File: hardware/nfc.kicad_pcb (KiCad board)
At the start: 2 copper layers, 85 x 50 mm, 61 parts, among them J1 CONN_01X03, P1 CON-SENSOR2, P2 BOOT, P3 DEBUG, U1 XMC130024, U2 PN7150, U3 DRILL, U4 DRILL, U5 DRILL, U6 DRILL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

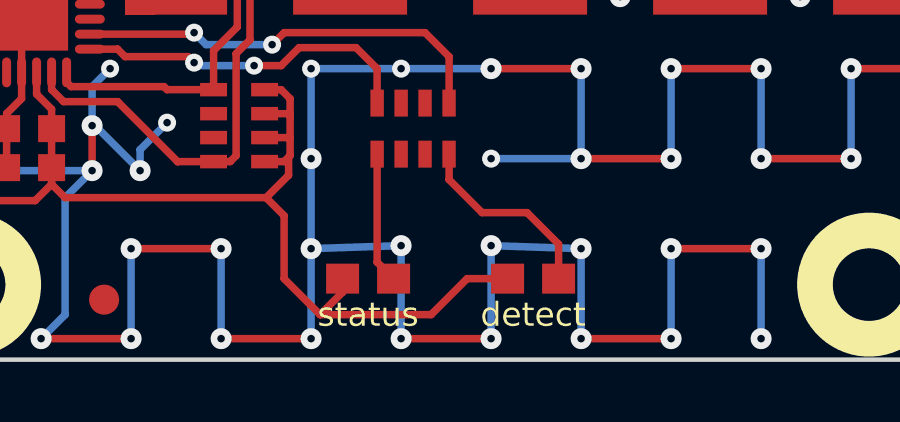
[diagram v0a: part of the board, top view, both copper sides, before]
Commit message: fix led text
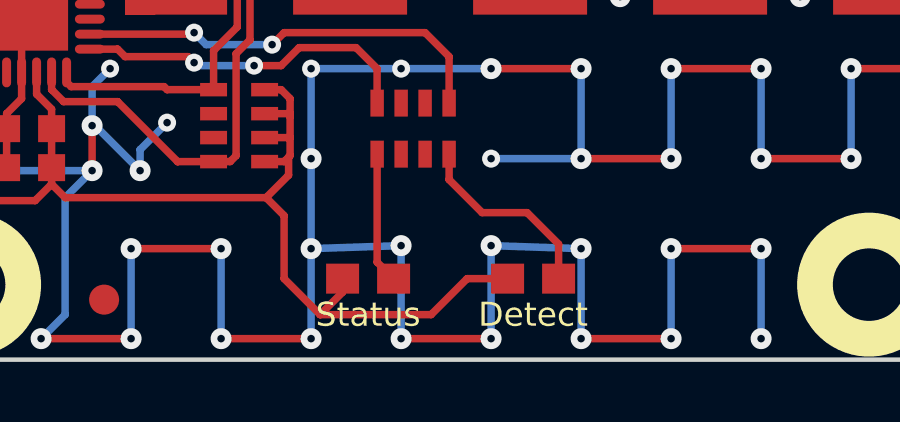
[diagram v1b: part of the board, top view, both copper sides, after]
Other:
- board text added: "Detect"
- board text added: "Status"
- board text removed: "detect"
- board text removed: "status"
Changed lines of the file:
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@@
-(kicad_pcb (version 4) (host pcbnew 4.0.2+dfsg1-stable)
+(kicad_pcb (version 4) (host pcbnew 4.0.7-e2-6376~61~ubuntu18.04.1)
   (general
     (links 136)
     (no_connects 0)
-    (area 110.324999 51.924999 195.475001 102.075001)
+    (area 109.544999 51.144999 275.89286 161.25)
     (thickness 1.6)
     (drawings 13)
@@
     )
   )
-  (gr_text detect (at 131.7 100.5) (layer F.SilkS)
+  (gr_text Detect (at 131.7 100.5) (layer F.SilkS)
     (effects (font (size 0.8 0.8) (thickness 0.15)))
   )
-  (gr_text status (at 126.2 100.5) (layer F.SilkS)
+  (gr_text Status (at 126.2 100.5) (layer F.SilkS)
     (effects (font (size 0.8 0.8) (thickness 0.15)))
   )

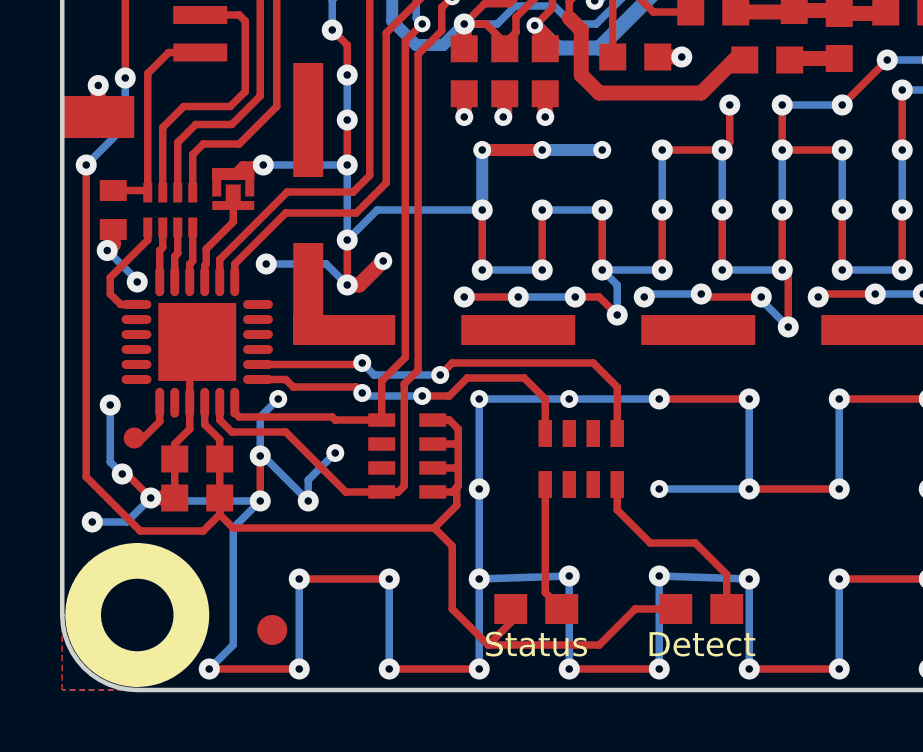
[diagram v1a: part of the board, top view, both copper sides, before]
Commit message: Change capacitor footprint(s) to C0402F
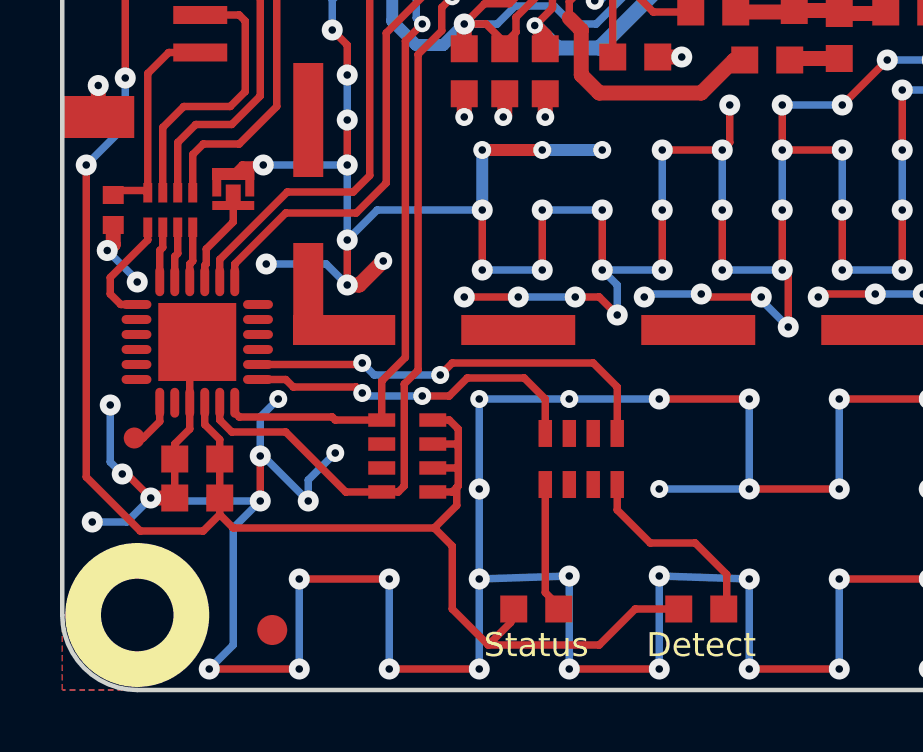
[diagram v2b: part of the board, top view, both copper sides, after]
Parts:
- ANT1: footprint NFC_ANTENNA_40_40 -> kicad-libraries:NFC_ANTENNA_40_40
- C1: footprint C0402E -> kicad-libraries:C0402F
- C10, C12, C13, C14, C15, C16, C17, C18, C19, C20, C21, C22, C23, C24, C25, C3, C4, C5, C6, C7, C8, C9: footprint C0603F -> kicad-libraries:C0603F
- D1, D2: footprint D0603E -> kicad-libraries:D0603F
- L1, L2, R1, R2, R3, R4, R5, R6: footprint R0603F -> kicad-libraries:R0603F
- RP2, RP3: footprint 4X0603 -> kicad-libraries:4X0603
- U3, U4, U5, U6, U7, U8: footprint DRILL_NP -> kicad-libraries:DRILL_NP
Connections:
- RP2 pad 6: (no net) -> Net-(RP2-Pad6)
- RP2 pad 7: (no net) -> Net-(RP2-Pad7)
- RP3 pad 2: (no net) -> Net-(RP3-Pad2)
- RP3 pad 3: (no net) -> Net-(RP3-Pad3)
- RP3 pad 6: (no net) -> Net-(RP3-Pad6)
- RP3 pad 7: (no net) -> Net-(RP3-Pad7)
- U1 pad 15: (no net) -> Net-(U1-Pad15)
- U1 pad 16: (no net) -> Net-(U1-Pad16)
- U1 pad 17: (no net) -> Net-(U1-Pad17)
- U1 pad 18: (no net) -> Net-(U1-Pad18)
- U1 pad 2: (no net) -> Net-(U1-Pad2)
- U1 pad 3: (no net) -> Net-(U1-Pad3)
- U1 pad 4: (no net) -> Net-(U1-Pad4)
- U1 pad 5: (no net) -> Net-(U1-Pad5)
- U1 pad 6: (no net) -> Net-(U1-Pad6)
- U1 pad 8: (no net) -> Net-(U1-Pad8)
- U2 pad 11: (no net) -> Net-(U2-Pad11)
- U2 pad 20: (no net) -> Net-(U2-Pad20)
- U2 pad 23: (no net) -> Net-(U2-Pad23)
- U2 pad 24: (no net) -> Net-(U2-Pad24)
- U2 pad 25: (no net) -> Net-(U2-Pad25)
- U2 pad 31: (no net) -> Net-(U2-Pad31)
- U2 pad 32: (no net) -> Net-(U2-Pad32)
- U2 pad 33: (no net) -> Net-(U2-Pad33)
- U2 pad 34: (no net) -> Net-(U2-Pad34)
- U2 pad 35: (no net) -> Net-(U2-Pad35)
- U2 pad 38: (no net) -> Net-(U2-Pad38)
- U2 pad 39: (no net) -> Net-(U2-Pad39)
- U2 pad 40: (no net) -> Net-(U2-Pad40)
